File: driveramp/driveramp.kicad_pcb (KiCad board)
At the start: 2 copper layers, 109 x 79 mm, 57 parts, among them J1 SMA, J2 SMA, P1 FAULT, P2 CONN_2, T1 MABA-011002, T2 2x Fair-Rite 2843006802, coax, U1 LM2936HVBMA-5.0, U2 MRFE6VP100H, U3 TL783

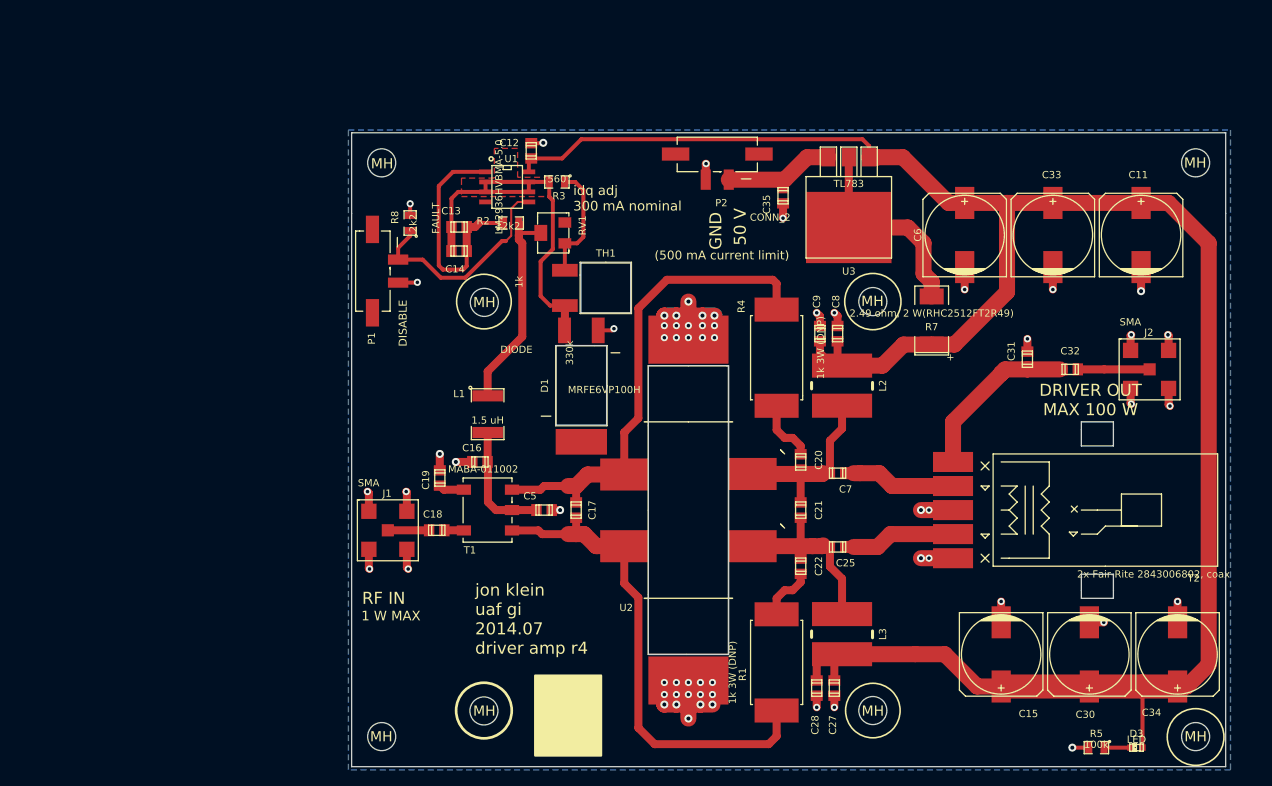
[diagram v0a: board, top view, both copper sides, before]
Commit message: switched driver amp current limiter to to-220 lm317hv, heatsink against al plate
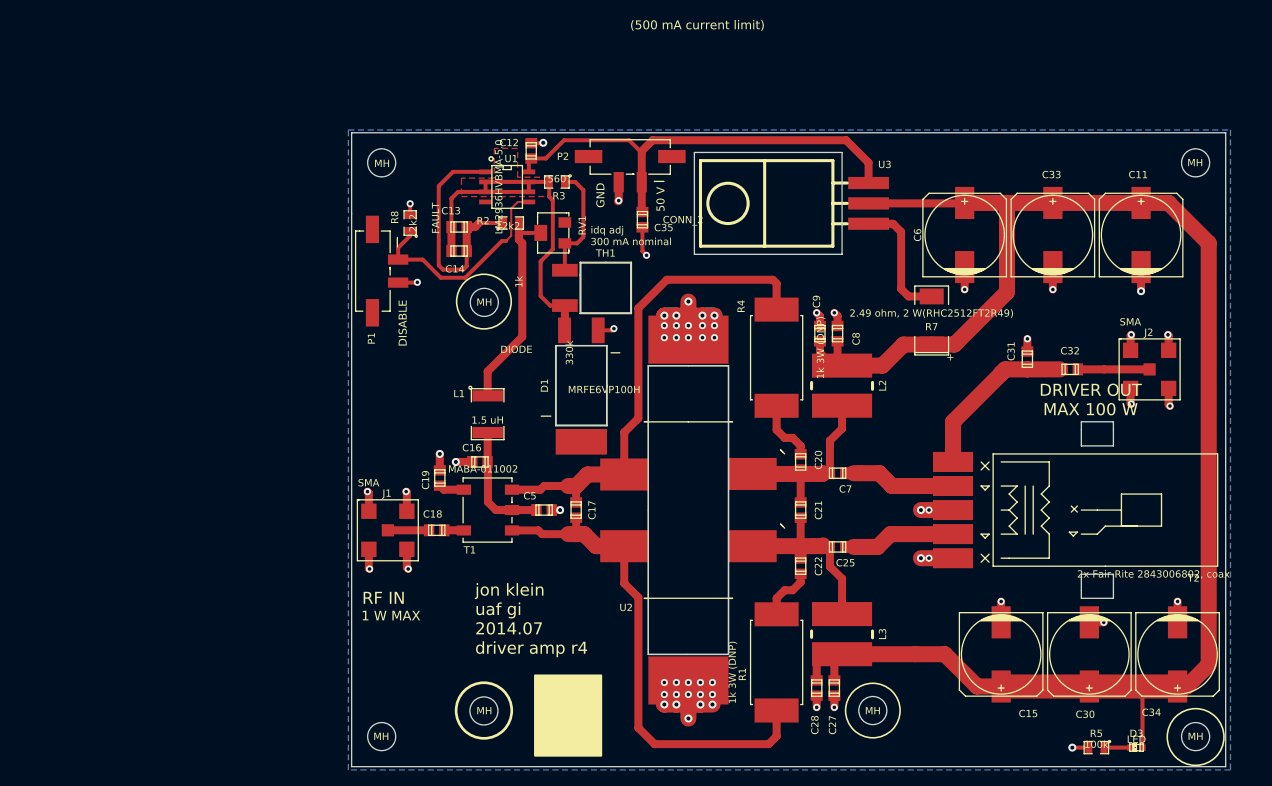
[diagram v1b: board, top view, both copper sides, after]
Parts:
- removed the MH at (141.0, 84.0)
- U3: value TL783 -> LM317HV; footprint SMD_Packages:DPAK3 -> to252_5:TO-220_Neutral123_Horizontal
- moved C35 17.8 mm to (112.3, 73.8)
- moved P2 10.9 mm to (110.7, 65.9)
- moved U3 6.00 mm to (139.7, 71.8), turned to 90 degrees
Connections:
- C12 pad 1: VDD -> /Vconn
- C35 pad 1: Net-(C35-Pad1) -> /Vconn
- P2 pad 1: Net-(C35-Pad1) -> /Vconn
- U1 pad 8: VDD -> /Vconn
- U3 pad 1: VDD -> Net-(R7-Pad2)
- U3 pad 2: Net-(R7-Pad2) -> VDD
- U3 pad 3: Net-(C35-Pad1) -> /Vconn
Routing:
- net /Vconn: track 0.00 -> 61.0 mm
- net VDD: track 258.9 -> 209.9 mm
- net Net-(R7-Pad2): track 38.1 -> 15.8 mm
- net Net-(C35-Pad1): track 14.7 -> 0.00 mm
- net GND: track 196.1 -> 198.4 mm
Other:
- outline, holes or cut-outs redrawn

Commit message: added matching network on driver amp board, modified footprint on transformer for easier soldering
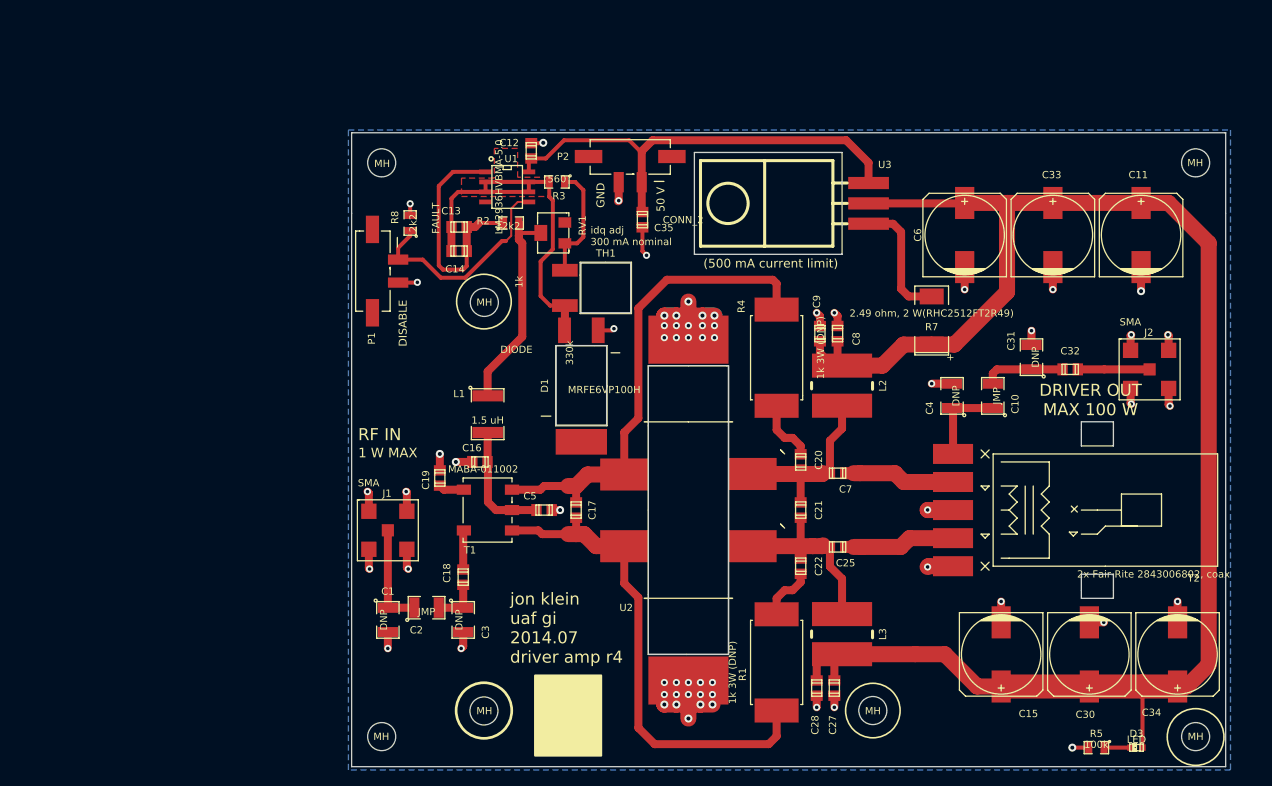
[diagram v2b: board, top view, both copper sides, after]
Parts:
- added C1: DNP, SMD_Packages:SMD-1210, F.Cu at (80.5, 123.7)
- added C10: JMP, SMD_Packages:SMD-1210, F.Cu at (156.0, 95.8)
- added C2: JMP, SMD_Packages:SMD-1210, F.Cu at (85.3, 122.2)
- added C3: DNP, SMD_Packages:SMD-1210, F.Cu at (89.9, 123.7)
- added C4: DNP, SMD_Packages:SMD-1210, F.Cu at (150.9, 95.8)
- C31: footprint Capacitors_SMD:c_0805 -> SMD_Packages:SMD-1210
- moved C18 6.71 mm to (89.9, 118.4), turned to 90 degrees
- moved C31 0.57 mm to (160.8, 90.9), turned to 90 degrees
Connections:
- C31 pad 1: Net-(C31-Pad1) -> Net-(C10-Pad2)
- C32 pad 1: Net-(C31-Pad1) -> Net-(C10-Pad2)
- J1 pad 1: Net-(C18-Pad2) -> Net-(C1-Pad1)
- T2 pad 5: Net-(C31-Pad1) -> Net-(C10-Pad1)
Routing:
- net Net-(C31-Pad1): track 22.4 -> 0.00 mm
- net Net-(C1-Pad1): track 0.00 -> 13.0 mm
- net Net-(C10-Pad1): track 0.00 -> 10.8 mm
- net Net-(C10-Pad2): track 0.00 -> 10.2 mm
- net GND: track 198.4 -> 201.7 mm, vias 63 -> 64
- net Net-(C18-Pad1): track 2.44 -> 4.93 mm
- net Net-(C18-Pad2): track 5.14 -> 5.91 mm

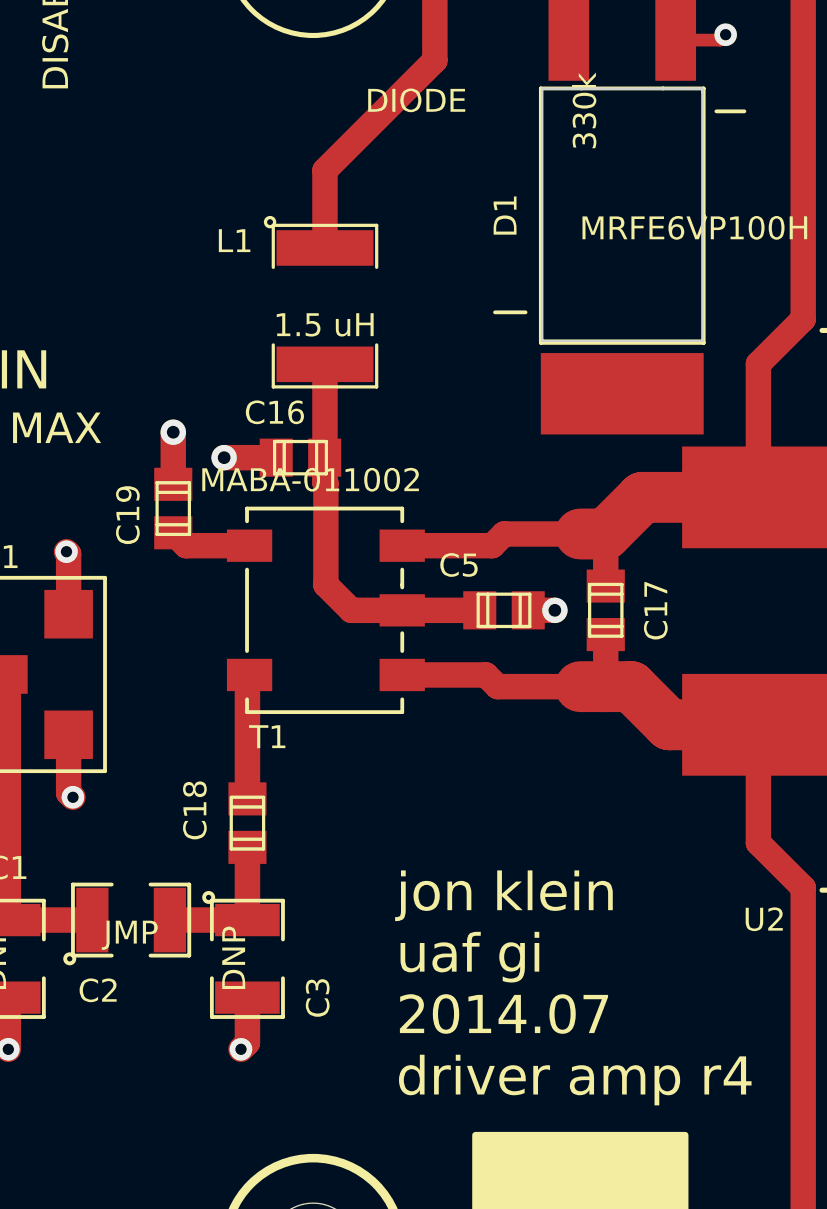
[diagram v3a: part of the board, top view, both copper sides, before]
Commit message: added extra decoupling to driver amp bias, specified fet ground connection
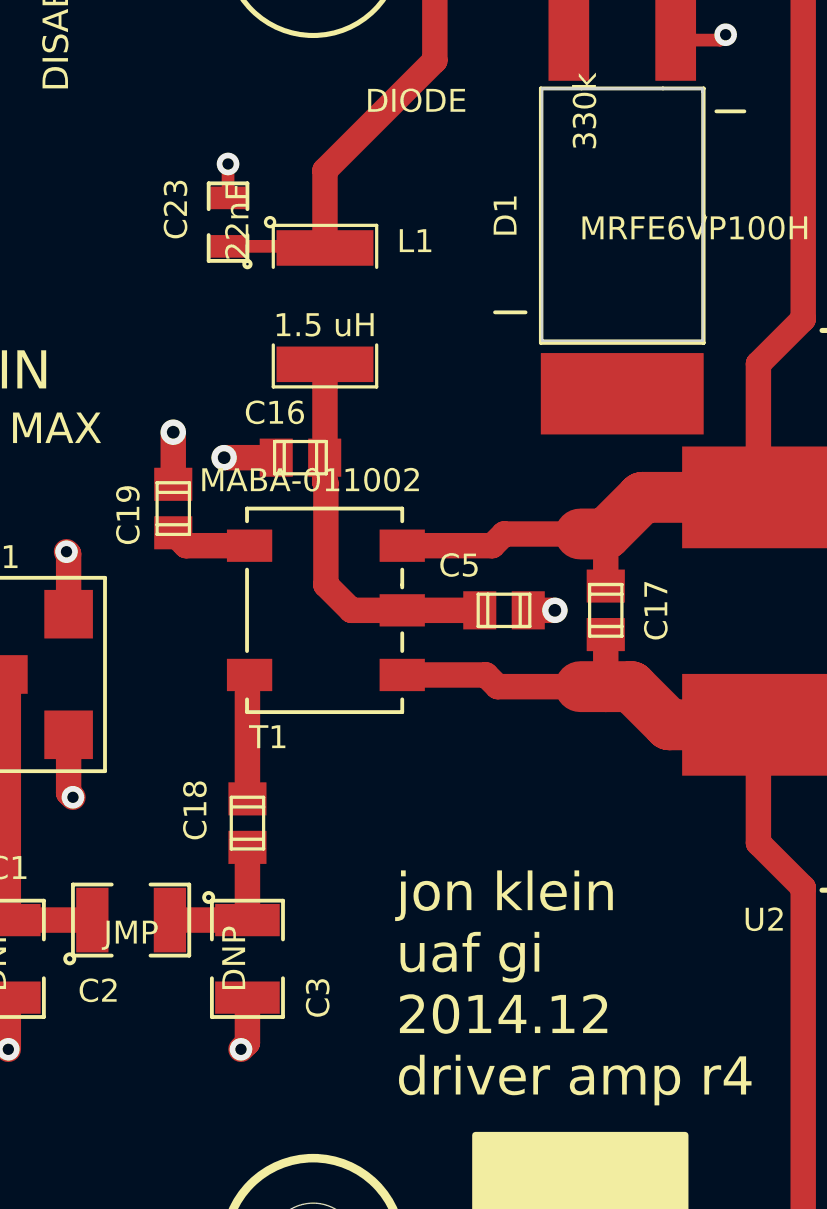
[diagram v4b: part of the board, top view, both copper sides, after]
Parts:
- added C23: 22nF, SMD_Packages:SMD-0805, F.Cu at (89.2, 94.7)
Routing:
- net Net-(C23-Pad1): track 26.5 -> 30.4 mm
- net GND: track 201.7 -> 203.1 mm, vias 64 -> 65
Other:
- board text added: "jon klein uaf gi 2014.12 driver amp r4"
- board text removed: "jon klein uaf gi 2014.07 driver amp r4"
